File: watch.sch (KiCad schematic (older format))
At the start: 80 parts, among them M1 3V3 35mA, Q1 IRLML6302, Q2 IRLML0060TRPbF, SW1 B3U-3000P, SW2 B3U-3000P, SW3 B3U-3000P, SW4 B3U-3000P, SW5 B3U-3000P, X1 MICROSD_SPI, X2 209E-BE01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

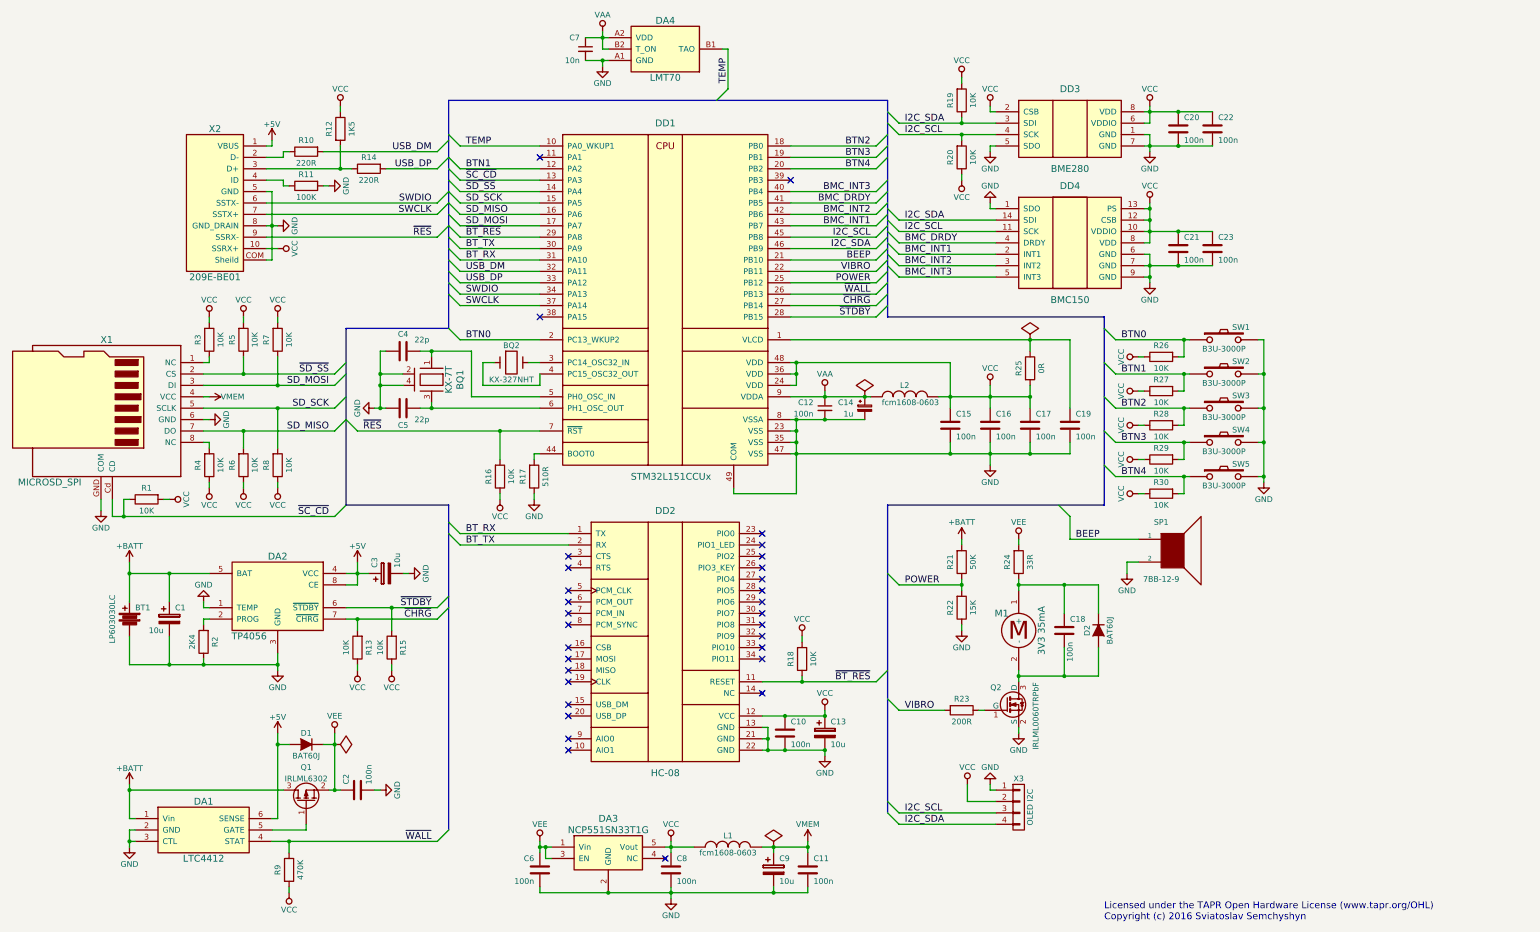
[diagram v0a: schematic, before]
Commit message: PCB finished, some changes in schematic
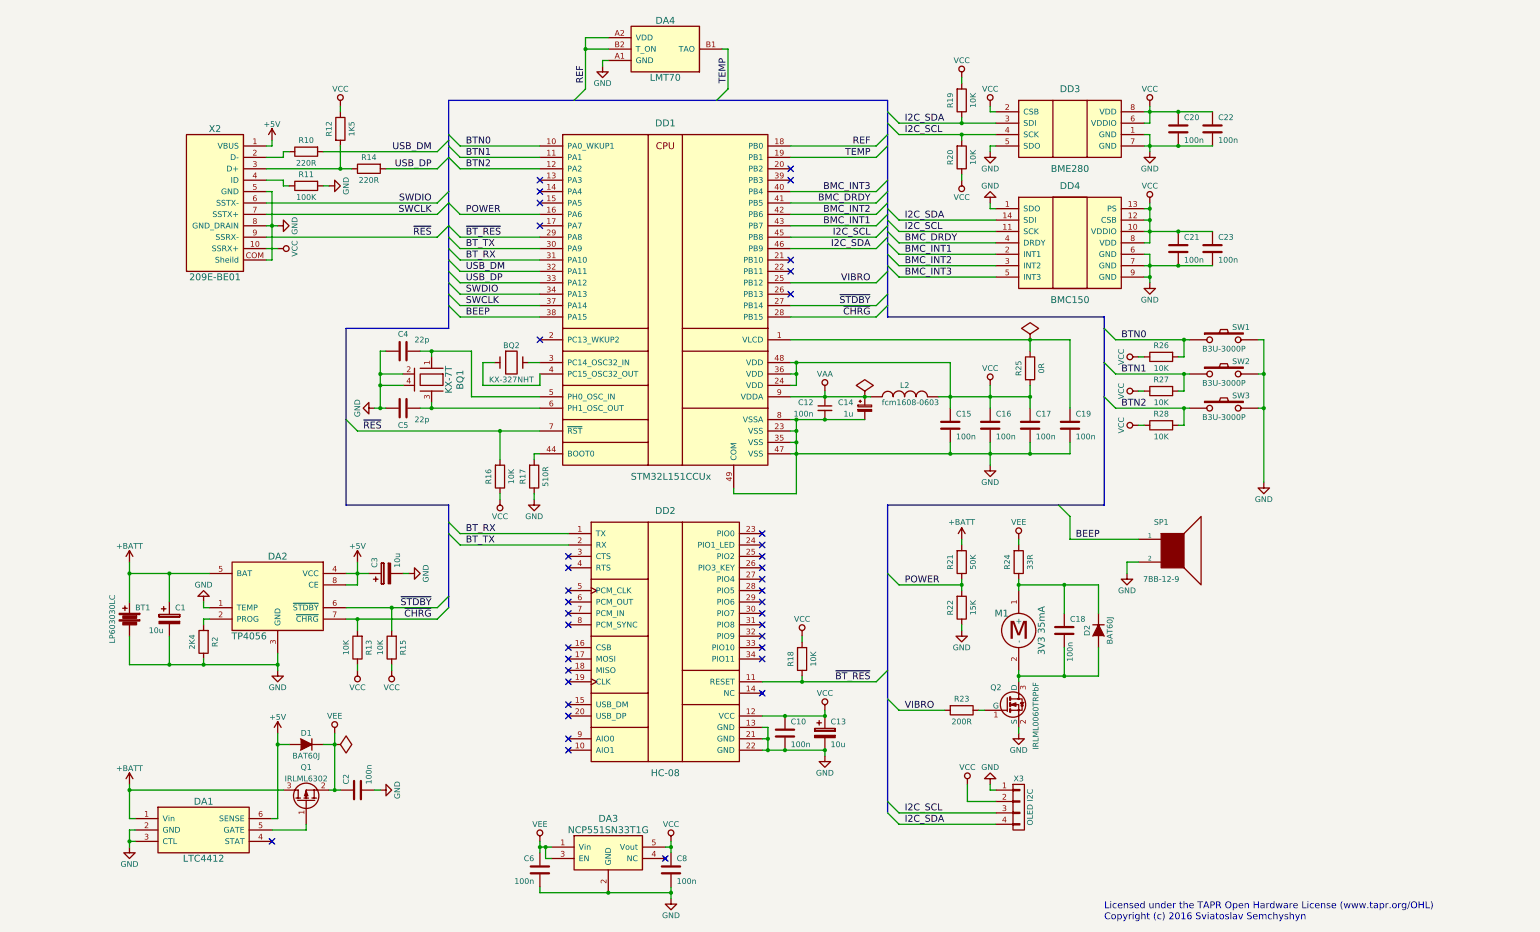
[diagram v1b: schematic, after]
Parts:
- removed C11: 100n, Capacitors_SMD:C_0402, symbol C
- removed C7: 10n, Capacitors_SMD:C_0402, symbol C_Small
- removed C9: 10u, Capacitors_SMD:C_0805, symbol CP
- removed L1: fcm1608-0603, Resistors_SMD:R_0603, symbol INDUCTOR
- removed R1, R29, R3, R30, R4, R5, R6, R7, R8: 10K, Resistors_SMD:R_0402, symbol R
- removed R9: 470K, Resistors_SMD:R_0402, symbol R
- removed SW4, SW5: B3U-3000P, Footprints:B3U-3000P, symbol SW_PUSH
- removed X1: MICROSD_SPI, Footprints:112J-TDAR-R01, symbol MICROSD_SPI
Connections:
- net BTN3 is gone; now on net TEMP: DD1.19 (PB1)
- net SD_MISO is gone; now on net POWER: DD1.16 (PA6)
- net BEEP: now also DD1.38 (PA15); no longer DD1.21 (PB10)
- net BTN0: now also DD1.10 (PA0_WKUP1); no longer DD1.2 (PC13_WKUP2)
- net BTN1: now also DD1.11 (PA1); no longer DD1.12 (PA2)
- net BTN2: now also DD1.12 (PA2); no longer DD1.18 (PB0)
- net POWER: no longer DD1.25 (PB12)
- net TEMP: no longer DD1.10 (PA0_WKUP1)
- net VAA: no longer DA4.A2 (VDD), DA4.B2 (T_ON)
- net VIBRO: now also DD1.25 (PB12); no longer DD1.22 (PB11)
- net ~CHRG: now also DD1.28 (PB15); no longer DD1.27 (PB14)
- net ~STDBY: now also DD1.27 (PB14); no longer DD1.28 (PB15)
- net BTN4: no longer names the net of DD1.20 (PB2)
- net SD_MOSI: no longer names the net of DD1.17 (PA7)
- net SD_SCK: no longer names the net of DD1.15 (PA5)
- net ~SC_CD: no longer names the net of DD1.13 (PA3)
- net ~SD_SS: no longer names the net of DD1.14 (PA4)
- net ~WALL: no longer names the net of DD1.26 (PB13)
- net ~WALL: no longer DA1.4 (STAT)
- new net REF: DA4.A2 (VDD), DA4.B2 (T_ON), DD1.18 (PB0)
- no-connect marks 31 -> 39

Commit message: Add flash connector for stm32f3discovery stlink
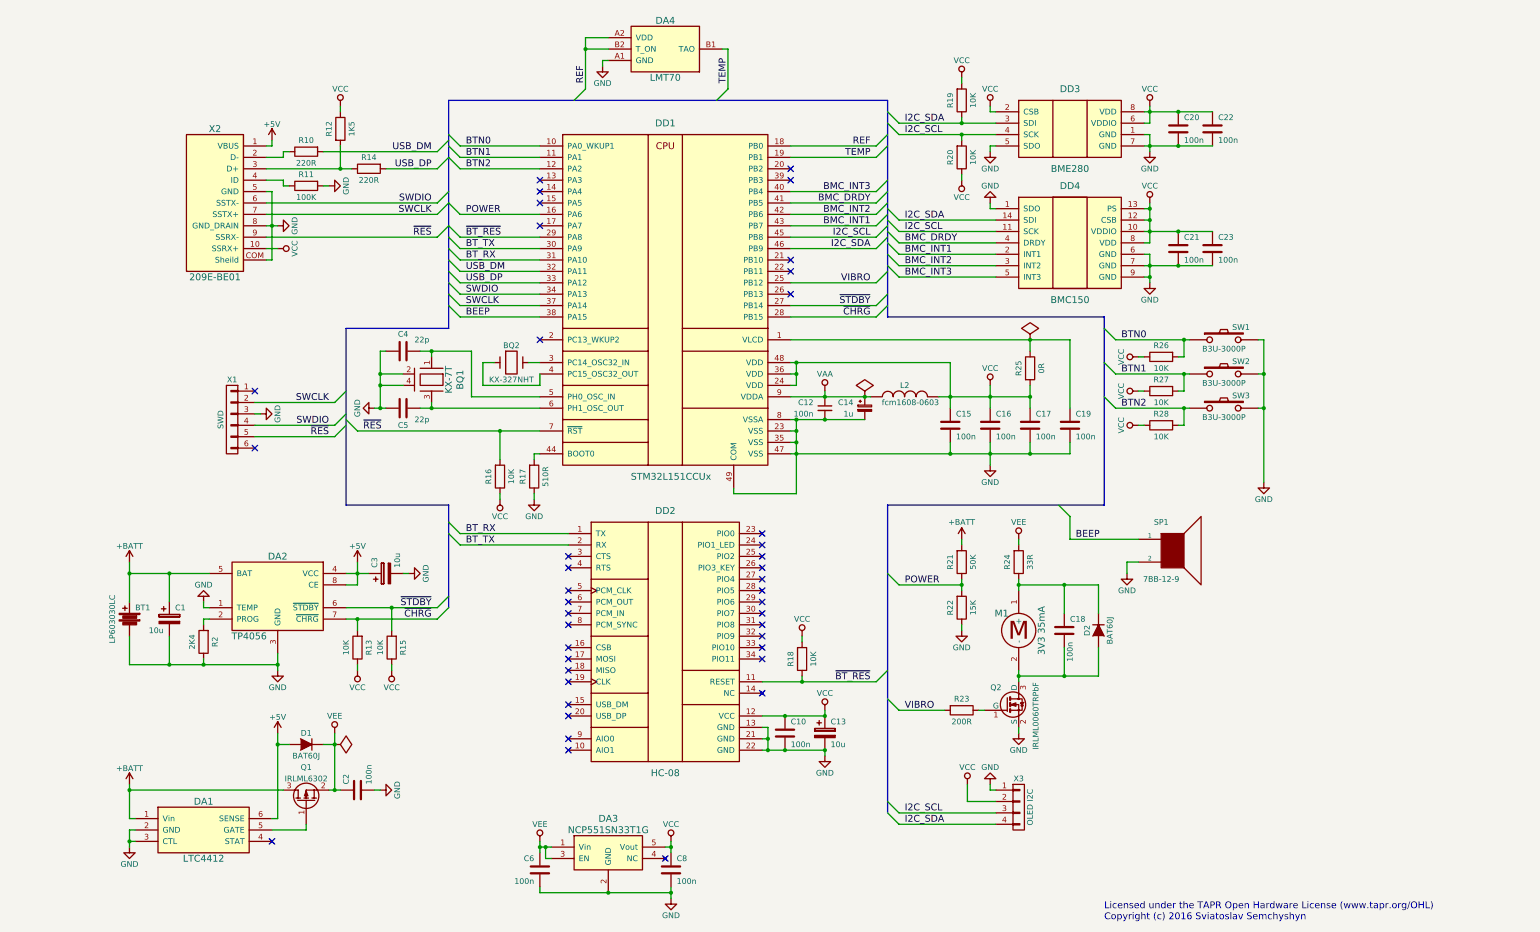
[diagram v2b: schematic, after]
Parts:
- added X1: SWD, Pin_Headers:Pin_Header_Straight_1x06, symbol CONN_01X06
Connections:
- net GND: now also X1.3 (P3)
- net SWCLK: now also X1.2 (P2)
- net SWDIO: now also X1.4 (P4)
- net ~RES: now also X1.5 (P5)
- no-connect marks 39 -> 41

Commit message: Fixed MCU footprint
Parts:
- DD1: footprint Housings_DFN_QFN:UQFN-48-1EP_6x6mm_Pitch0.4mm -> Housings_DFN_QFN:QFN-48-1EP_7x7mm_Pitch0.5mm
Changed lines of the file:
@@
 F 0 "DD1" H 8300 4900 60  0000 C CNN
 F 1 "STM32L151CCUx" H 8350 1800 60  0000 C CNN
-F 2 "Housings_DFN_QFN:UQFN-48-1EP_6x6mm_Pitch0.4mm" H 8300 4350 60  0001 C CNN
+F 2 "Housings_DFN_QFN:QFN-48-1EP_7x7mm_Pitch0.5mm" H 8300 4350 60  0001 C CNN
 F 3 "" H 8300 4350 60  0000 C CNN
 	1    8300 3350
